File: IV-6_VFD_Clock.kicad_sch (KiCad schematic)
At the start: 0 parts

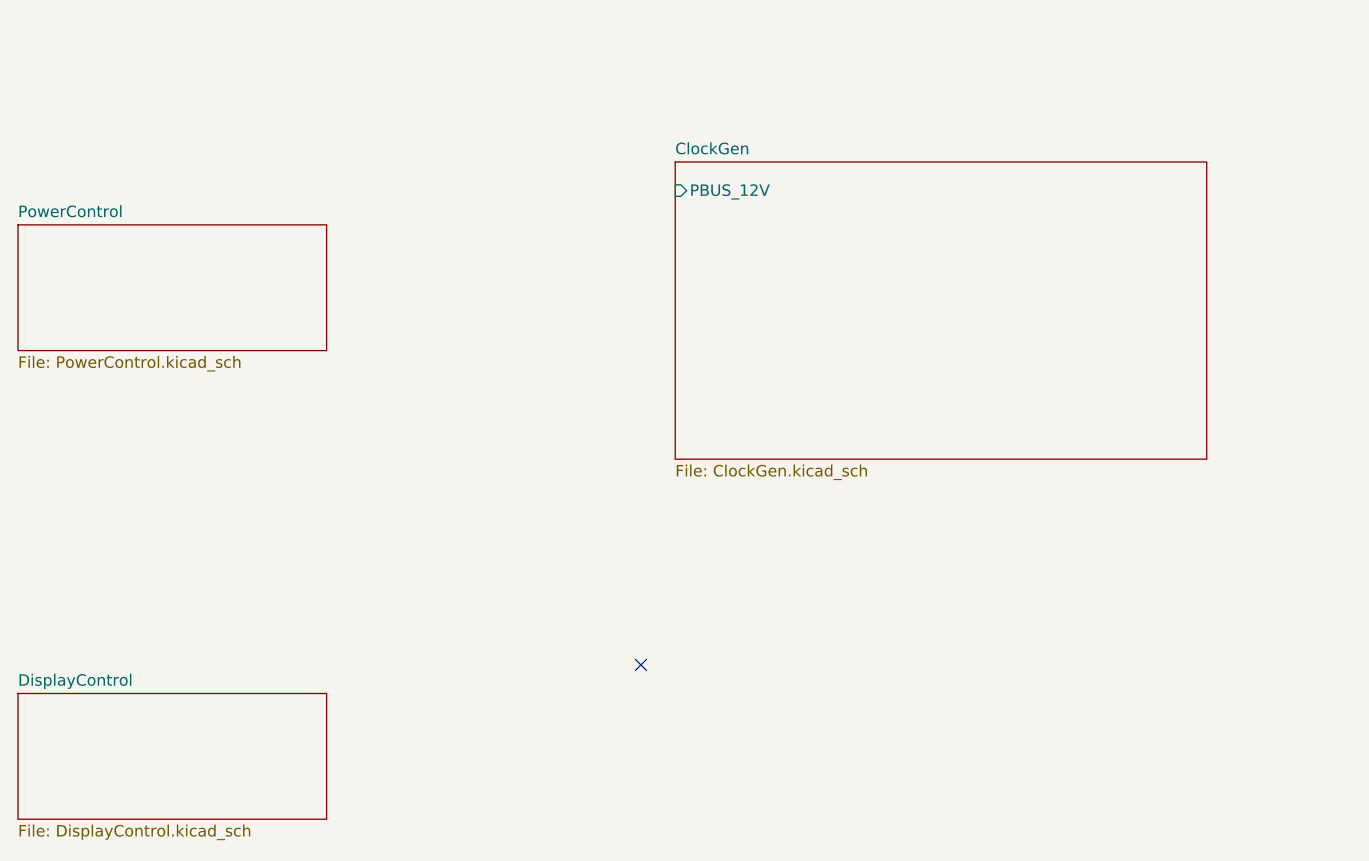
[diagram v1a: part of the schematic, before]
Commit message: Started refactor of display section
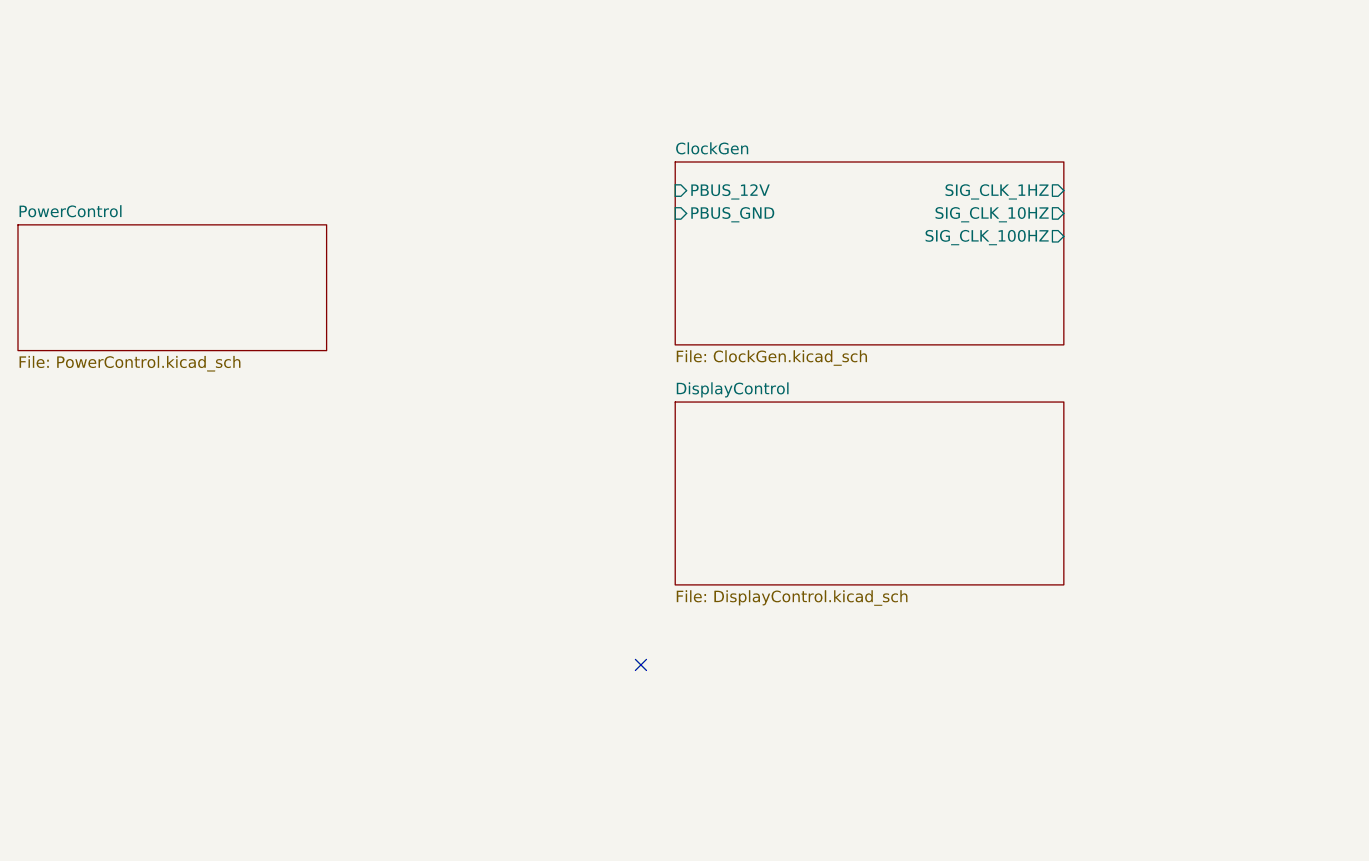
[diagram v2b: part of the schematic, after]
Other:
- sheet ClockGen ports: added PBUS_GND, SIG_CLK_100HZ, SIG_CLK_10HZ, SIG_CLK_1HZ; removed none
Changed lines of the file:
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@@
 	(title_block
 		(title "IV-6 VFD Clock")
-		(date "2025-06-23")
+		(date "2025-06-25")
 		(rev "MkII")
 		(company "ADBeta")
@@
 	)
 	(sheet
-		(at 34.925 161.925)
-		(size 34.29 13.97)
+		(at 107.95 129.54)
+		(size 43.18 20.32)
 		(exclude_from_sim no)
 		(in_bom yes)
@@
 		)
 		(property "Sheetname" "DisplayControl"
-			(at 34.925 161.2134 0)
+			(at 107.95 128.8284 0)
 			(effects
 				(font
@@
 		)
 		(property "Sheetfile" "DisplayControl.kicad_sch"
-			(at 34.925 176.4796 0)
+			(at 107.95 150.4446 0)
 			(effects
 				(font
@@
 	(sheet
 		(at 107.95 102.87)
-		(size 59.055 33.02)
+		(size 43.18 20.32)
 		(exclude_from_sim no)
 		(in_bom yes)
@@
 		)
 		(property "Sheetfile" "ClockGen.kicad_sch"
-			(at 107.95 136.4746 0)
+			(at 107.95 123.7746 0)
 			(effects
 				(font
@@
 			(effects
 				(font
+					(size 1.27 1.27)
+				)
+				(justify left)
+			)
+		)
+		(pin "SIG_CLK_1HZ" output
+			(at 151.13 106.045 0)
+			(effects
+				(font
+					(size 1.27 1.27)
+				)
+				(justify right)
+			)
+		)
+		(pin "SIG_CLK_10HZ" output
+			(at 151.13 108.585 0)
+			(effects
+				(font
+					(size 1.27 1.27)
+				)
+				(justify right)
+			)
+		)
+		(pin "SIG_CLK_100HZ" output
+			(at 151.13 111.125 0)
+			(effects
+				(font
+					(size 1.27 1.27)
+				)
+				(justify right)
+			)
+		)
+		(pin "PBUS_GND" input
+			(at 107.95 108.585 180)
+			(effects
+				(font

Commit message: Started PCB Outline & PSU
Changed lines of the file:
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@@
 	(title_block
 		(title "IV-6 VFD Clock")
-		(date "2025-06-25")
+		(date "2025-07-01")
 		(rev "MkII")
 		(company "ADBeta")
@@
 	)
 	(sheet
-		(at 34.925 109.855)
-		(size 34.29 13.97)
+		(at 60.325 102.235)
+		(size 43.18 20.32)
 		(exclude_from_sim no)
 		(in_bom yes)
@@
 		)
 		(property "Sheetname" "PowerControl"
-			(at 34.925 109.1434 0)
+			(at 60.325 101.5234 0)
 			(effects
 				(font
@@
 		)
 		(property "Sheetfile" "PowerControl.kicad_sch"
-			(at 34.925 124.4096 0)
+			(at 60.325 123.1396 0)
 			(effects
 				(font

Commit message: PSU Design started
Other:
- sheet PowerControl ports: added PBUS_12v, PBUS_GND, PBUS_SW_12v, PBUS_SW_6v, VFD_HTR_A, VFD_HTR_B; removed none
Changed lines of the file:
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@@
 	(title_block
 		(title "IV-6 VFD Clock")
-		(date "2025-07-01")
+		(date "2025-07-06")
 		(rev "MkII")
 		(company "ADBeta")
@@
 			)
 		)
+		(pin "PBUS_12v" output
+			(at 103.505 106.045 0)
+			(effects
+				(font
+					(size 1.27 1.27)
+				)
+				(justify right)
+			)
+		)
+		(pin "PBUS_GND" output
+			(at 103.505 108.585 0)
+			(effects
+				(font
+					(size 1.27 1.27)
+				)
+				(justify right)
+			)
+		)
+		(pin "PBUS_SW_6v" output
+			(at 103.505 118.745 0)
+			(effects
+				(font
+					(size 1.27 1.27)
+				)
+				(justify right)
+			)
+		)
+		(pin "PBUS_SW_12v" output
+			(at 103.505 116.205 0)
+			(effects
+				(font
+					(size 1.27 1.27)
+				)
+				(justify right)
+			)
+		)
+		(pin "VFD_HTR_A" output
+			(at 60.325 106.045 180)
+			(effects
+				(font
+					(size 1.27 1.27)
+				)
+				(justify left)
+			)
+		)
+		(pin "VFD_HTR_B" output
+			(at 60.325 108.585 180)
+			(effects
+				(font
+					(size 1.27 1.27)
+				)
+				(justify left)
+			)
+		)
